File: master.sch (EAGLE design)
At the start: 67 parts, among them IC2 MCP1703-3302, M1 DHT22-NP, M2 NRF24L01P-M, Q1 IRLML2502, Q3 25MHz, SW1 EC11E_SW, U1 XMEGA-A3TQFP, U2 DS1302SOIC, U3 25LC640A-E/SN, U4 ENC28J60SO, X1 serial, X2 SPI/1W, X3 I2C, X4 ADC, X6 PS25_3W-R, X7 PS25_3W-R, X8 PS25_3W-R, X9 PS25_3W-R

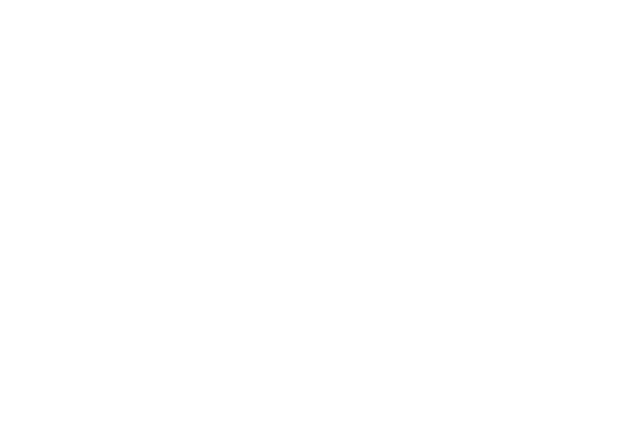
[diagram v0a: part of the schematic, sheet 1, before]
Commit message: added license+version information
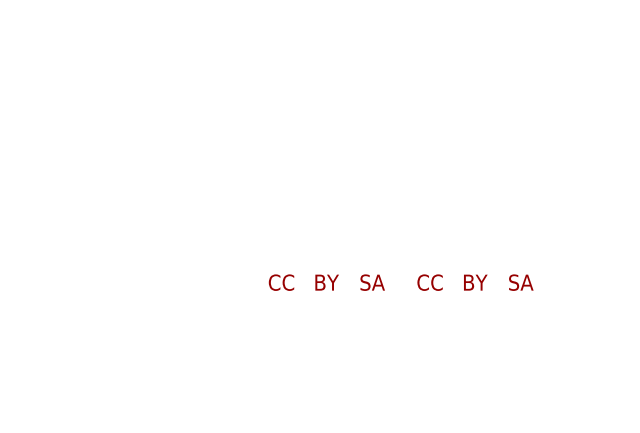
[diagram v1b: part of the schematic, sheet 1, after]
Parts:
- added U$1: CC-TPLACE-HALF, creative-commons:CC-TPLACE-HALF
- added U$10: SA-TOP-HALF, creative-commons:SA-TOP-HALF
- added U$2: BY-TPLACE-HS, creative-commons:BY-TPLACE-HS
- added U$7: SA-TPLACE-HALF, creative-commons:SA-TPLACE-HALF
- added U$8: CC-TOP-HALF, creative-commons:CC-TOP-HALF
- added U$9: BY-TOP-HALF, creative-commons:BY-TOP-HALF

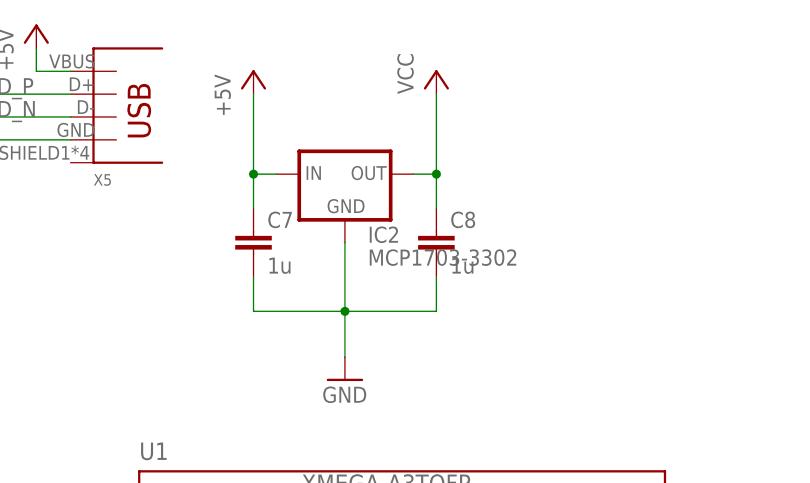
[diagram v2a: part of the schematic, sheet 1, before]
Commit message: improved routing
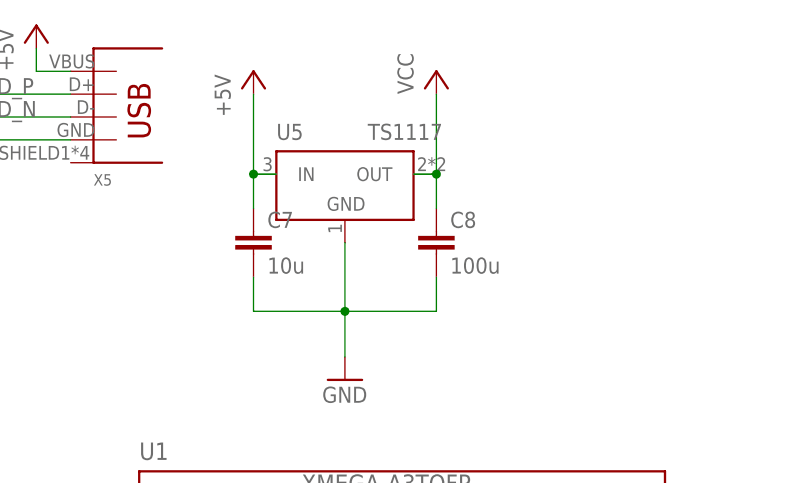
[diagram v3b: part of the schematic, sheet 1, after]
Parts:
- removed IC2: MCP1703-3302, karlnet-parts:MCP1700SOT89
- added U5: TS1117, TS1117:TS1117
- C7: value 1u -> 10u; device rcl:C-EUC0603 -> rcl:C-EUC1206; _REICHELT_ (none) -> X7R-G1206 10/16
- C8: value 1u -> 100u; device rcl:C-EUC0603 -> rcl:C-EUC1210; _REICHELT_ (none) -> X5R-G1210 100
- renumbered SW1 to S1
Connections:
- net +5V: now also U5.IN; no longer IC2.IN
- net GND: now also U5.GND; no longer IC2.GND
- net VCC: now also U5.OUT; no longer IC2.OUT
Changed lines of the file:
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@@
 <part name="R1" library="rcl" deviceset="R-EU_" device="R0603" value="10k"/>
 <part name="GND10" library="supply1" deviceset="GND" device=""/>
-<part name="C7" library="rcl" deviceset="C-EU" device="C0603" value="1u"/>
-<part name="C8" library="rcl" deviceset="C-EU" device="C0603" value="1u"/>
+<part name="C7" library="rcl" deviceset="C-EU" device="C1206" value="10u">
+<attribute name="_REICHELT_" value="X7R-G1206 10/16"/>
+</part>
+<part name="C8" library="rcl" deviceset="C-EU" device="C1210" value="100u">
+<attribute name="_REICHELT_" value="X5R-G1210 100"/>
+</part>
 <part name="P+9" library="supply1" deviceset="+5V" device=""/>
 <part name="Q2" library="crystal" deviceset="CRYSTAL" device="TC26H"/>
@@
 <part name="U2" library="adafruit" deviceset="DS1302" device="SOIC" value="DS1302SOIC"/>
 <part name="GND11" library="supply1" deviceset="GND" device=""/>
-<part name="IC2" library="karlnet-parts" deviceset="MCP1700" device="SOT89" value="MCP1703-3302"/>
 <part name="U3" library="microchip" deviceset="25LC640A-E/SN" device=""/>
 <part name="P+6" library="supply1" deviceset="VCC" device=""/>
@@
 <part name="R3" library="rcl" deviceset="R-EU_" device="R0603" value="10K"/>
 <part name="S2" library="jt-switches" deviceset="MEC-SWITCH" device="SMT"/>
-<part name="SW1" library="switch-alps" deviceset="EC11E_SW" device=""/>
+<part name="S1" library="switch-alps" deviceset="EC11E_SW" device=""/>
 <part name="X6" library="con_PS25" deviceset="PS25_3W" device="-R" value="PS25_3W-R"/>
 <part name="X7" library="con_PS25" deviceset="PS25_3W" device="-R" value="PS25_3W-R"/>
@@
 <part name="U$9" library="creative-commons" deviceset="BY" device="-TOP-HALF" value="BY-TOP-HALF"/>
 <part name="U$10" library="creative-commons" deviceset="SA" device="-TOP-HALF" value="SA-TOP-HALF"/>
+<part name="U5" library="TS1117" deviceset="TS1117" device=""/>
 </parts>
 <sheets>
@@
 <instance part="R1" gate="G$1" x="35.56" y="45.72" rot="R180"/>
 <instance part="GND10" gate="1" x="69.85" y="133.35"/>
-<instance part="C7" gate="G$1" x="59.69" y="149.86"/>
-<instance part="C8" gate="G$1" x="80.01" y="149.86"/>
+<instance part="C7" gate="G$1" x="59.69" y="149.86">
+<attribute name="_REICHELT_" x="59.69" y="149.86" size="1.778" layer="96" display="off"/>
+</instance>
+<instance part="C8" gate="G$1" x="80.01" y="149.86">
+<attribute name="_REICHELT_" x="80.01" y="149.86" size="1.778" layer="96" display="off"/>
+</instance>
 <instance part="P+9" gate="1" x="59.69" y="167.64"/>
 <instance part="Q2" gate="G$1" x="220.98" y="167.64" rot="MR0"/>
@@
 <instance part="U2" gate="G$1" x="223.52" y="149.86"/>
 <instance part="GND11" gate="1" x="223.52" y="132.08"/>
-<instance part="IC2" gate="1" x="69.85" y="156.21"/>
 <instance part="U3" gate="A" x="226.06" y="107.95"/>
 <instance part="P+6" gate="VCC" x="80.01" y="167.64"/>
@@
 <instance part="U$9" gate="G$1" x="238.76" y="20.32"/>
 <instance part="U$10" gate="G$1" x="243.84" y="20.32"/>
+<instance part="U5" gate="G$1" x="69.85" y="153.67"/>
 </instances>
 <busses>
 </busses>
 <nets>
-<net name="GND" class="0">
+<net name="GND" class="1">
 <segment>
 <wire x1="59.69" y1="140.97" x2="69.85" y2="140.97" width="0.1524" layer="91"/>
@@
 <pinref part="C7" gate="G$1" pin="2"/>
 <pinref part="C8" gate="G$1" pin="2"/>
-<pinref part="IC2" gate="1" pin="GND"/>
+<pinref part="U5" gate="G$1" pin="GND"/>
 </segment>
 <segment>
@@
 <junction x="59.69" y="156.21"/>
 <pinref part="P+9" gate="1" pin="+5V"/>
-<pinref part="IC2" gate="1" pin="IN"/>
+<pinref part="U5" gate="G$1" pin="IN"/>
 </segment>
 <segment>
@@
 <wire x1="80.01" y1="156.21" x2="80.01" y2="165.1" width="0.1524" layer="91"/>
 <junction x="80.01" y="156.21"/>
-<pinref part="IC2" gate="1" pin="OUT"/>
 <pinref part="P+6" gate="VCC" pin="VCC"/>
+<pinref part="U5" gate="G$1" pin="OUT"/>
 </segment>
 <segment>
@@
 <instance part="R3" gate="G$1" x="73.66" y="138.43" rot="R90"/>
 <instance part="S2" gate="G$1" x="134.62" y="128.27"/>
-<instance part="SW1" gate="G$1" x="138.43" y="116.84" rot="R90"/>
-<instance part="SW1" gate="G$2" x="135.89" y="102.87"/>
+<instance part="S1" gate="G$1" x="138.43" y="116.84" rot="R90"/>
+<instance part="S1" gate="G$2" x="135.89" y="102.87"/>
 <instance part="X6" gate="-1" x="86.36" y="130.81" rot="R270"/>
 <instance part="X6" gate="-2" x="64.77" y="153.67"/>
@@
 <instance part="R15" gate="G$1" x="83.82" y="76.2"/>
 <instance part="GND25" gate="1" x="91.44" y="73.66"/>
-<instance part="SW1" gate="G$3" x="140.97" y="107.95" rot="R180"/>
-<instance part="SW1" gate="G$4" x="140.97" y="110.49" rot="R180"/>
+<instance part="S1" gate="G$3" x="140.97" y="107.95" rot="R180"/>
+<instance part="S1" gate="G$4" x="140.97" y="110.49" rot="R180"/>
 </instances>
 <busses>
 </busses>
 <nets>
-<net name="GND" class="0">
+<net name="GND" class="1">
 <segment>
 <pinref part="GND6" gate="1" pin="GND"/>
@@
 <junction x="140.97" y="116.84"/>
 <wire x1="140.97" y1="116.84" x2="140.97" y2="110.49" width="0.1524" layer="91"/>
-<pinref part="SW1" gate="G$1" pin="C"/>
-<pinref part="SW1" gate="G$2" pin="1"/>
+<pinref part="S1" gate="G$1" pin="C"/>
+<pinref part="S1" gate="G$2" pin="1"/>
 <junction x="140.97" y="102.87"/>
-<pinref part="SW1" gate="G$3" pin="G"/>
+<pinref part="S1" gate="G$3" pin="G"/>
 <junction x="140.97" y="107.95"/>
-<pinref part="SW1" gate="G$4" pin="G"/>
+<pinref part="S1" gate="G$4" pin="G"/>
 <junction x="140.97" y="110.49"/>
 <wire x1="140.97" y1="110.49" x2="140.97" y2="107.95" width="0.1524" layer="91"/>
@@
 <wire x1="130.81" y1="119.38" x2="121.92" y2="119.38" width="0.1524" layer="91"/>
 <label x="121.92" y="119.38" size="1.778" layer="95"/>
-<pinref part="SW1" gate="G$1" pin="B"/>
+<pinref part="S1" gate="G$1" pin="B"/>
 </segment>
 </net>
@@
 <wire x1="130.81" y1="114.3" x2="121.92" y2="114.3" width="0.1524" layer="91"/>
 <label x="121.92" y="114.3" size="1.778" layer="95"/>
-<pinref part="SW1" gate="G$1" pin="A"/>
+<pinref part="S1" gate="G$1" pin="A"/>
 </segment>
 </net>
@@
 <wire x1="130.81" y1="102.87" x2="121.92" y2="102.87" width="0.1524" layer="91"/>
 <label x="121.92" y="102.87" size="1.778" layer="95"/>
-<pinref part="SW1" gate="G$2" pin="2"/>
-</segment>
-</net>
+<pinref part="S1" gate="G$2" pin="2"/>
+</segment>
+</net>

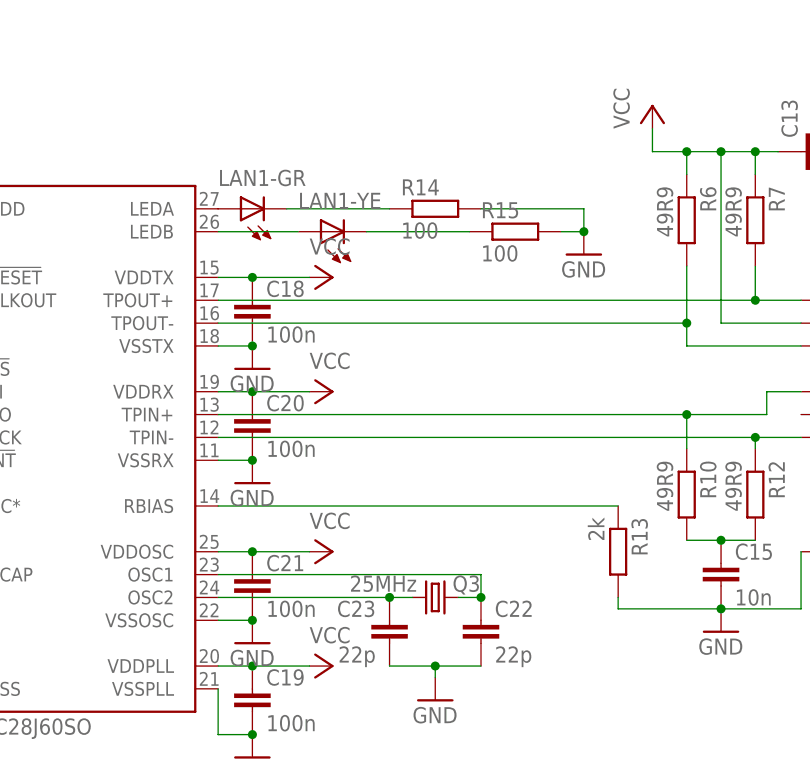
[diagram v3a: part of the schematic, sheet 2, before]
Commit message: added sd card interface
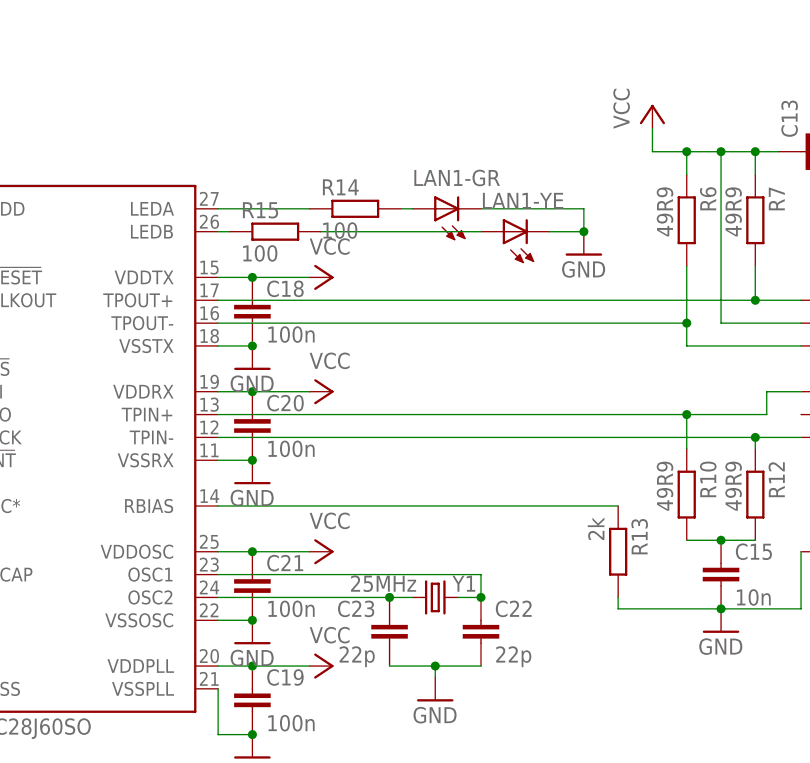
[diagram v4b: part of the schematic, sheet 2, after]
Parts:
- added SD1: MICROSD_SW, sd:MICROSD_SW
- renumbered Q2 to Y2, Q3 to Y1
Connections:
- new net !SDCS: SD1-SD.!SS, U1.PE3(OC0D/TXD0)
- new net SDCD: SD1-CD.CD2, U1.PE4(OC1A/!SS!)
- net !EEPCS: now also U1.PF1(OC0B/XCK0); no longer U1.PF0(OC0A)
- net !EEPHOLD: now also U1.PF0(OC0A); no longer U1.PF1(OC0B/XCK0)
- net GND: now also LAN1-GR.C, LAN1-YE.C, SD1-CD.CD1, SD1-SD.GND, SD1-SHIELD.SHIELD; no longer R14.2, R15.2
- net MISO: now also SD1-SD.DO
- net MOSI: now also SD1-SD.DI
- net N$21: now also R14.1; no longer LAN1-GR.A
- net N$22: now also R15.1; no longer LAN1-YE.A
- net N$23: now also LAN1-GR.A, R14.2; no longer LAN1-GR.C, R14.1
- net N$24: now also LAN1-YE.A, R15.2; no longer LAN1-YE.C, R15.1
- net RTC_CE: now also U1.PF5; no longer U1.PE4(OC1A/!SS!)
- net RTC_CLK: now also U1.PF6; no longer U1.PE2(OC0C/RXD0)
- net RTC_IO: now also U1.PF4; no longer U1.PE3(OC0D/TXD0)
- net SCK: now also SD1-SD.SCK
- net VCC: now also SD1-SD.VCC
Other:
- moved on the sheet: LAN1-GR, LAN1-YE, R14, R15
